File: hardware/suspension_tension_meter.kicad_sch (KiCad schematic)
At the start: 18 parts, among them J1 Conn_01x04, J2 Conn_01x06, J3 Conn_01x04, J4 Conn_01x04, SW1 Tactswitch, U1 STM32L4P5RET6, Y1 16MHz

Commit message: Arrange footprints
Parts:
- J1: footprint Connector_PinHeader_1.00mm:PinHeader_1x04_P1.00mm_Vertical_SMD_Pin1Left -> Connector_Wire:SolderWire-0.25sqmm_1x04_P4.2mm_D0.65mm_OD1.7mm_Relief
- J2: footprint Connector_PinHeader_1.00mm:PinHeader_1x06_P1.00mm_Vertical_SMD_Pin1Left -> Connector_PinHeader_2.54mm:PinHeader_1x06_P2.54mm_Vertical_SMD_Pin1Left
- J3, J4: footprint Connector_PinHeader_1.00mm:PinHeader_1x04_P1.00mm_Vertical_SMD_Pin1Left -> Connector_JST:JST_EH_S5B-EH_1x05_P2.50mm_Horizontal; symbol Connector_Generic:Conn_01x04 -> Connector_Generic:Conn_01x05
- SW1: footprint Button_Switch_SMD:SW_Push_1P1T_NO_6x6mm_H9.5mm -> Button_Switch_SMD:SW_SPST_PTS645
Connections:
- net GND: now also J3.5 (Pin_5), J4.5 (Pin_5)
- net SWO: now reaches J2.6 (Pin_6)
- net SWO: now also U1.55 (PB3)
- no-connect marks 40 -> 38
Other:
- note added: "SHLD"
- moved on the sheet: C1, C2, C3, C4, C5, J1, J2

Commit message: Apply PUTM branding
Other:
- company: PUT Motorsport -> Author: I. Kajdan
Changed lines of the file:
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@@
   (title_block
     (title "Push-rods Suspension Tension Meter")
-    (date "2022-12-10")
+    (date "2022-12-11")
     (rev "${REVISION}")
-    (company "PUT Motorsport")
-    (comment 3 "Reviewer:")
-    (comment 4 "Author: I. Kajdan")
+    (company "Author: I. Kajdan")
   )
   (junction (at 87.63 50.8) (diameter 0) (color 0 0 0 0)

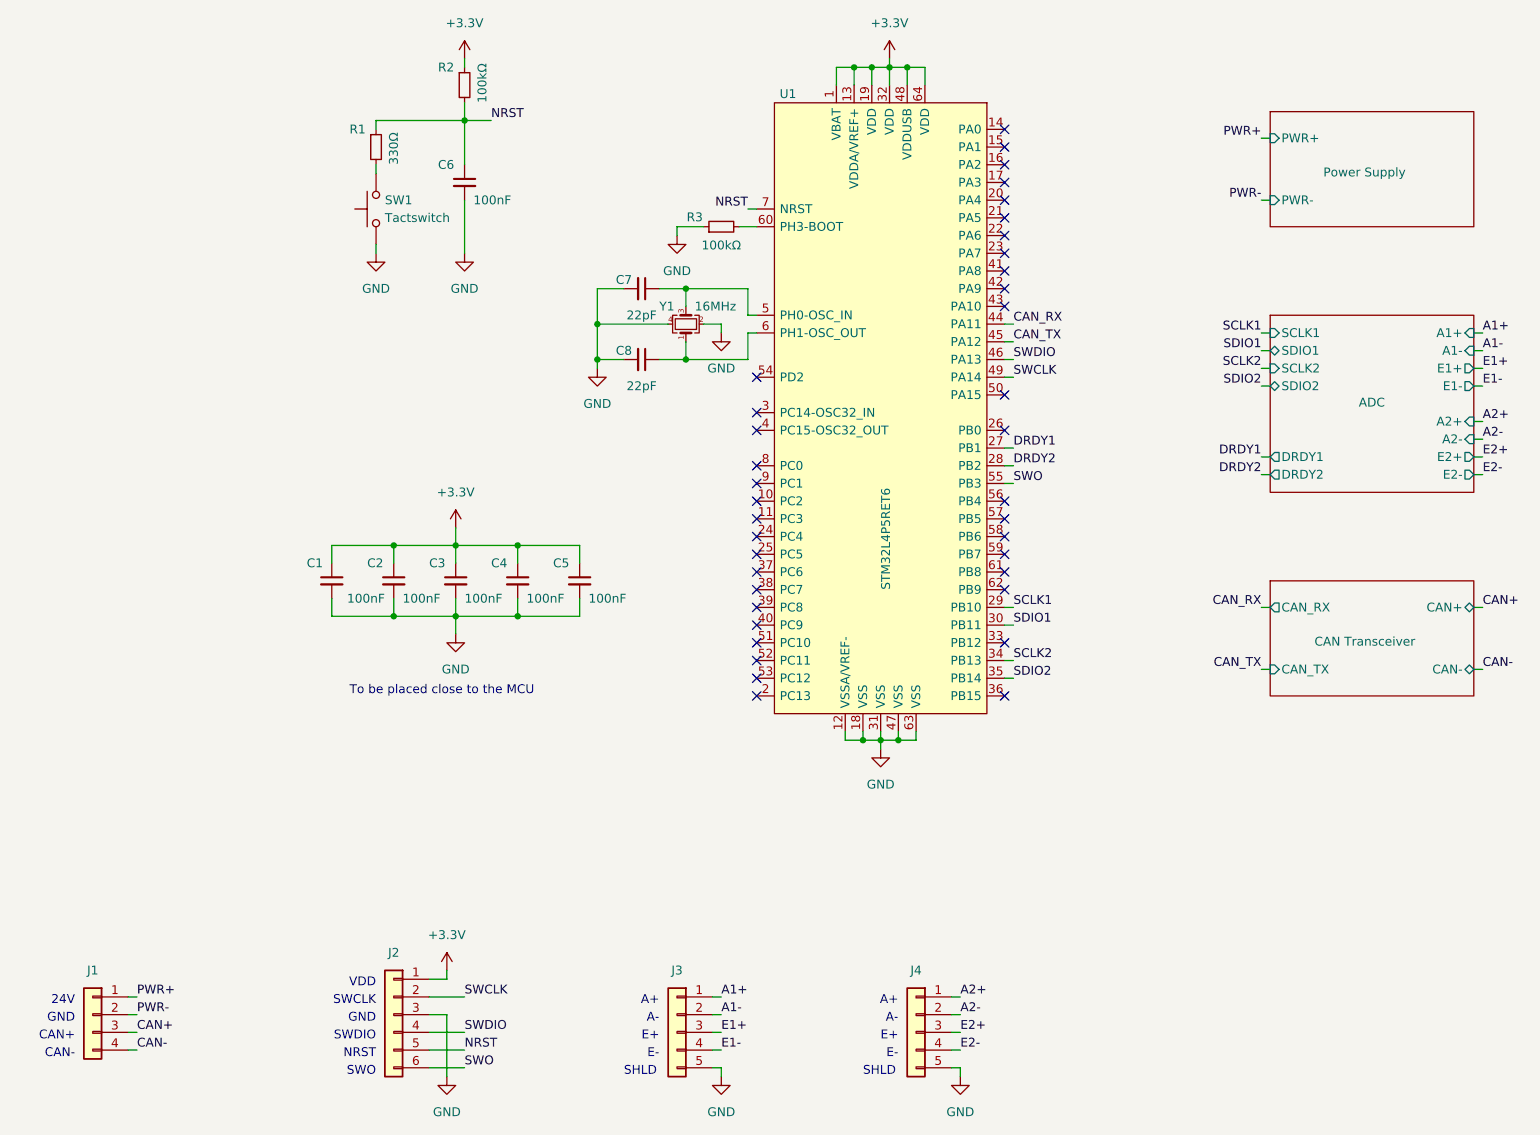
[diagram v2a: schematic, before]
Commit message: Miscellaneous changes
- Use THT connectors
- Adjust ADC circuit according to the datasheet
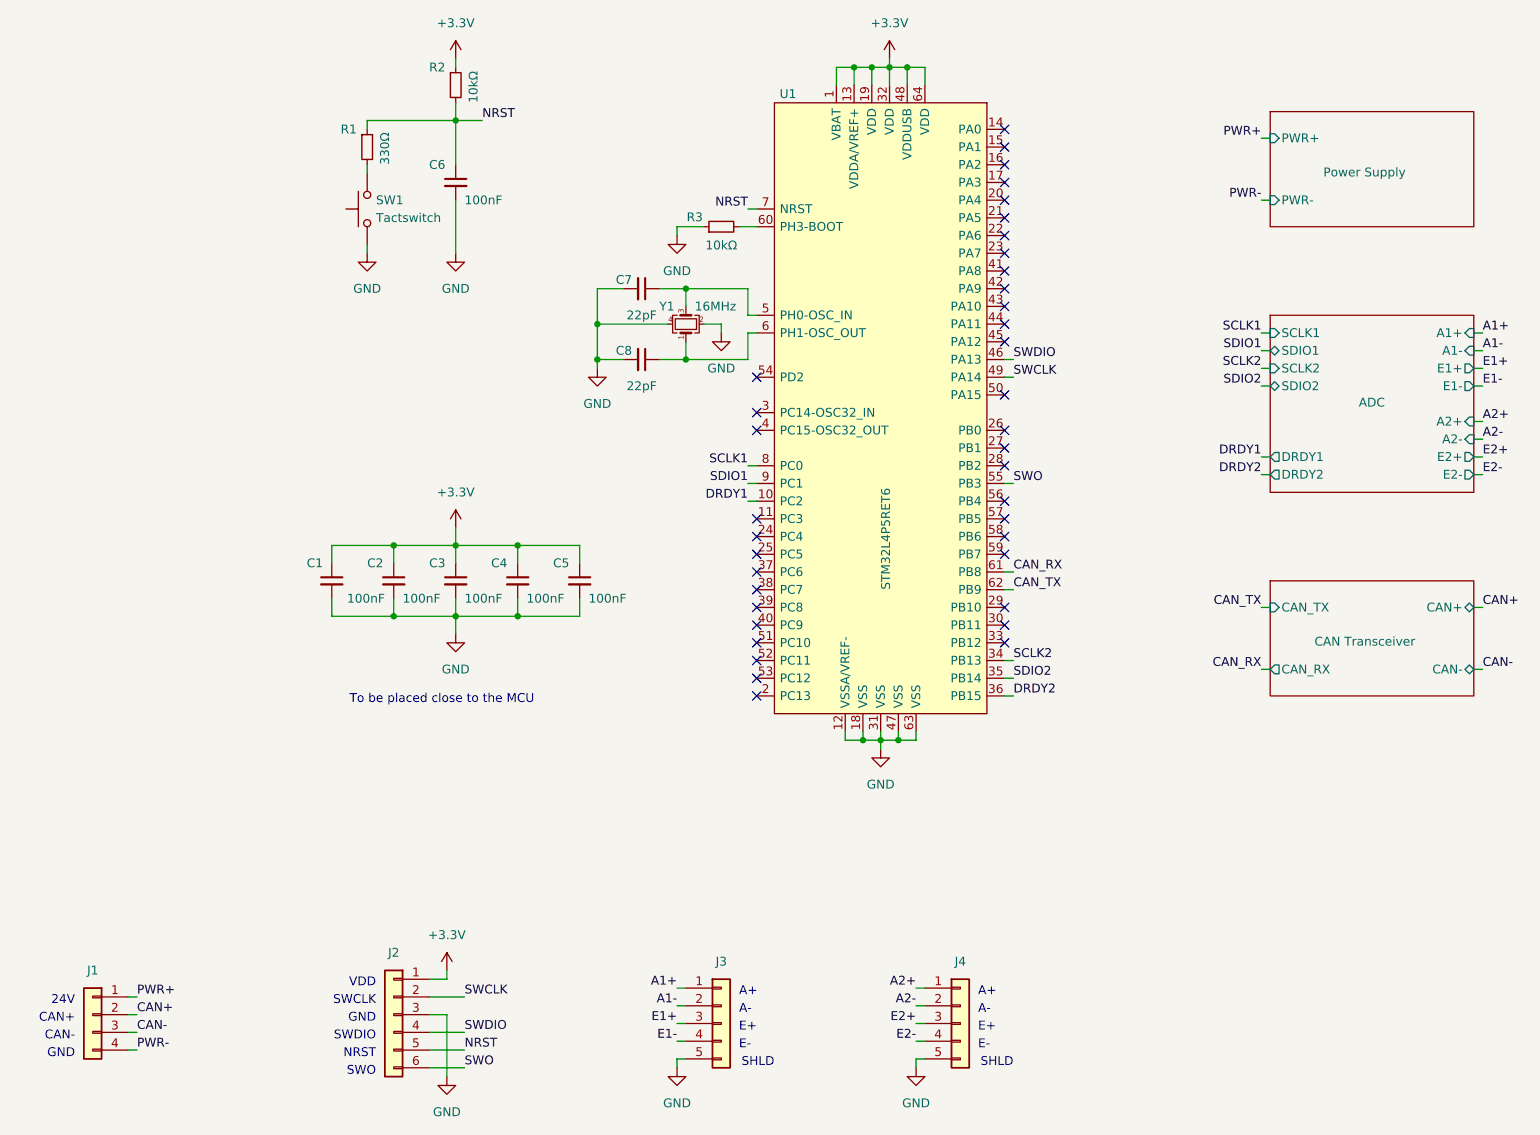
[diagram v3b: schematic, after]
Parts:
- J1: now left out of the parts list
- J2: footprint Connector_PinHeader_2.54mm:PinHeader_1x06_P2.54mm_Vertical_SMD_Pin1Left -> Connector_PinHeader_2.54mm:PinHeader_1x06_P2.54mm_Vertical
- J3, J4: footprint Connector_JST:JST_EH_S5B-EH_1x05_P2.50mm_Horizontal -> Connector_Molex:Molex_PicoBlade_53048-0510_1x05_P1.25mm_Horizontal
- R2, R3: value 100kΩ -> 10kΩ
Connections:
- net CAN+: now also J1.2 (Pin_2); no longer J1.3 (Pin_3)
- net CAN-: now also J1.3 (Pin_3); no longer J1.4 (Pin_4)
- net CAN_RX: now also U1.61 (PB8); no longer U1.44 (PA11)
- net CAN_TX: now also U1.62 (PB9); no longer U1.45 (PA12)
- net DRDY1: now also U1.10 (PC2); no longer U1.27 (PB1)
- net DRDY2: now also U1.36 (PB15); no longer U1.28 (PB2)
- net PWR-: now also J1.4 (Pin_4); no longer J1.2 (Pin_2)
- net SCLK1: now also U1.8 (PC0); no longer U1.29 (PB10)
- net SDIO1: now also U1.9 (PC1); no longer U1.30 (PB11)
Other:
- moved on the sheet: C6, J3, J4, R1, R2, SW1

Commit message: Route PCB tracks
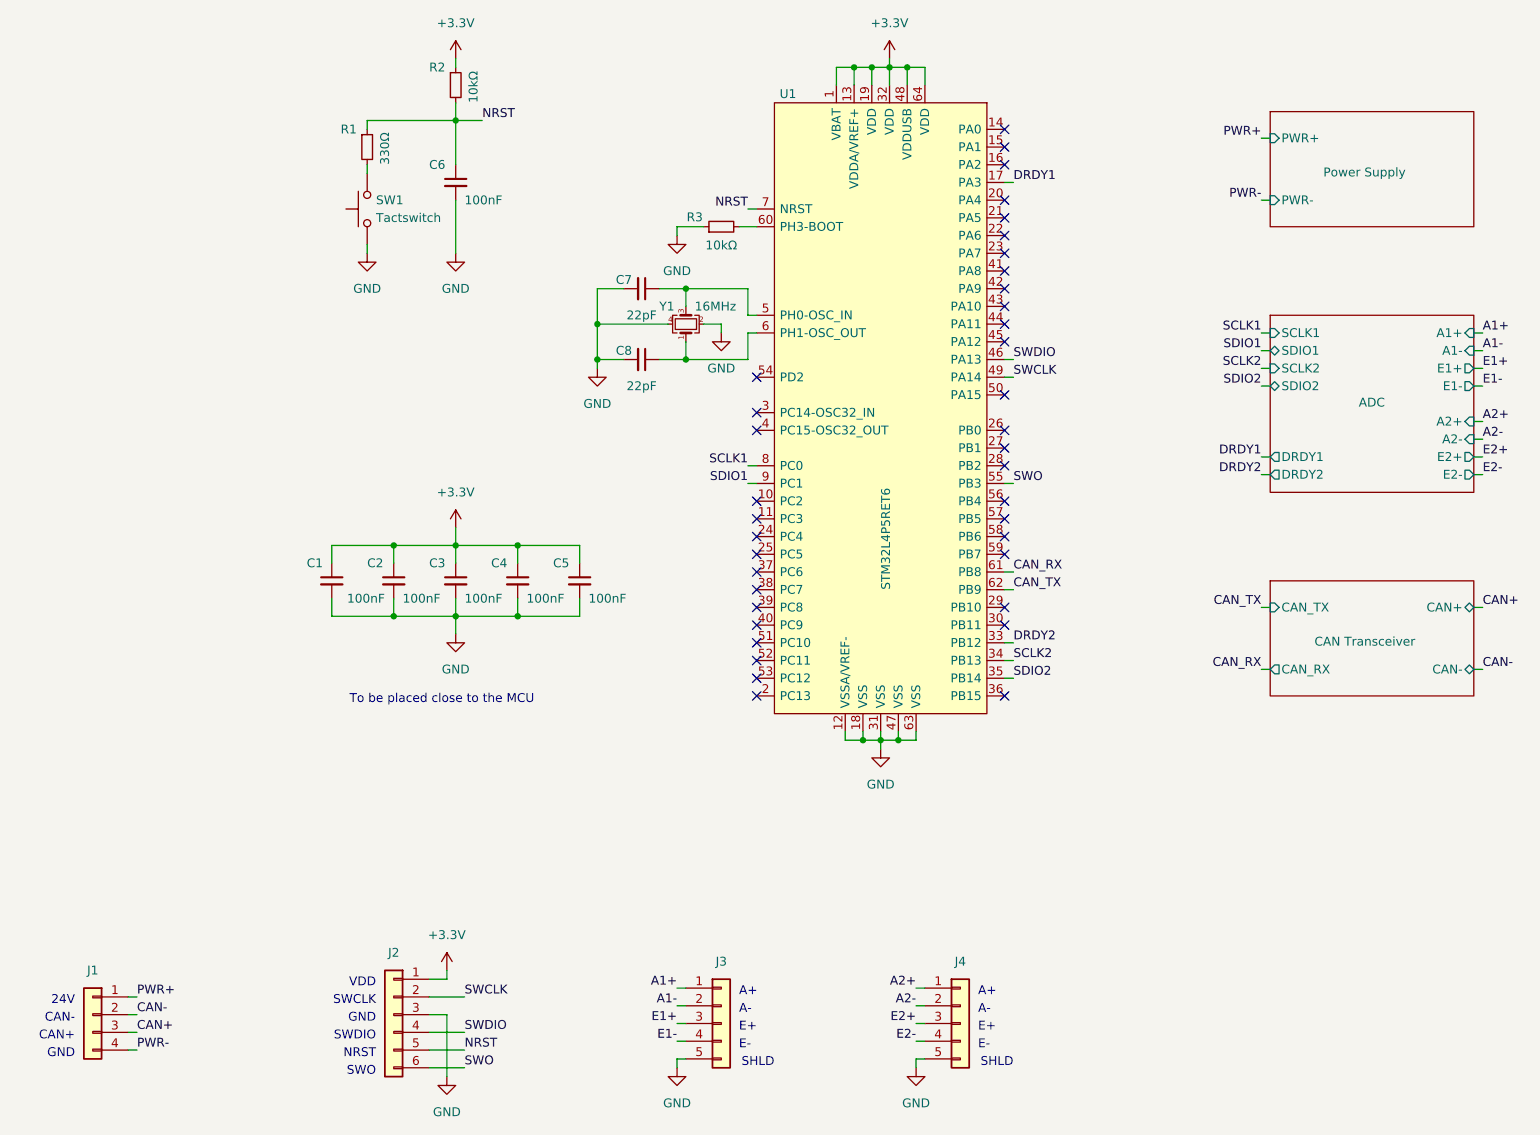
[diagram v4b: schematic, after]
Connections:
- net CAN+: now also J1.3 (Pin_3); no longer J1.2 (Pin_2)
- net CAN-: now also J1.2 (Pin_2); no longer J1.3 (Pin_3)
- net DRDY1: now also U1.17 (PA3); no longer U1.10 (PC2)
- net DRDY2: now also U1.33 (PB12); no longer U1.36 (PB15)
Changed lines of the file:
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@@
   (title_block
     (title "Push-rods Suspension Tension Meter")
-    (date "2022-12-11")
+    (date "2022-12-18")
     (rev "${REVISION}")
     (company "Author: I. Kajdan")
@@
   (no_connect (at 165.1 100.33))
   (no_connect (at 165.1 97.79))
-  (no_connect (at 165.1 125.73))
   (no_connect (at 165.1 123.19))
   (no_connect (at 165.1 120.65))
@@
   (no_connect (at 165.1 95.25))
   (no_connect (at 165.1 54.61))
-  (no_connect (at 165.1 57.15))
   (no_connect (at 165.1 52.07))
   (no_connect (at 165.1 62.23))
   (no_connect (at 165.1 64.77))
-  (no_connect (at 165.1 59.69))
   (no_connect (at 165.1 74.93))
   (no_connect (at 165.1 67.31))
@@
   (no_connect (at 165.1 72.39))
   (no_connect (at 165.1 77.47))
+  (no_connect (at 165.1 57.15))
+  (no_connect (at 165.1 133.35))
   (no_connect (at 165.1 82.55))
+  (no_connect (at 129.54 105.41))
   (wire (pts (xy 149.86 139.7) (xy 149.86 138.43))
     (stroke (width 0) (type default) (color 0 0 0 0))
@@
     (stroke (width 0) (type default) (color 0 0 0 0))
   )
+  (wire (pts (xy 165.1 59.69) (xy 166.37 59.69))
+    (stroke (width 0) (type default) (color 0 0 0 0))
+  )
   (wire (pts (xy 121.92 80.01) (xy 124.46 80.01))
     (stroke (width 0) (type default) (color 0 0 0 0))
@@
     (stroke (width 0) (type default) (color 0 0 0 0))
   )
-  (wire (pts (xy 166.37 133.35) (xy 165.1 133.35))
+  (wire (pts (xy 166.37 125.73) (xy 165.1 125.73))
     (stroke (width 0) (type default) (color 0 0 0 0))
   )
@@
     (stroke (width 0) (type default) (color 0 0 0 0))
   )
-  (wire (pts (xy 129.54 105.41) (xy 128.27 105.41))
-    (stroke (width 0) (type default) (color 0 0 0 0))
-  )
   (wire (pts (xy 86.36 121.92) (xy 77.47 121.92))
     (stroke (width 0) (type default) (color 0 0 0 0))
@@
     (effects (font (size 1.27 1.27)) (justify left bottom))
   )
-  (text "CAN+" (at 31.75 180.34 180)
+  (text "CAN+" (at 31.75 182.88 180)
     (effects (font (size 1.27 1.27)) (justify right bottom))
   )
@@
     (effects (font (size 1.27 1.27)) (justify left bottom))
   )
-  (text "CAN-" (at 31.75 182.88 180)
+  (text "CAN-" (at 31.75 180.34 180)
     (effects (font (size 1.27 1.27)) (justify right bottom))
   )
@@
     (effects (font (size 1.27 1.27)) (justify left bottom))
   )
-  (label "CAN+" (at 40.64 179.07 0)
+  (label "CAN-" (at 40.64 179.07 0)
     (effects (font (size 1.27 1.27)) (justify left bottom))
   )
@@
     (effects (font (size 1.27 1.27)) (justify right bottom))
   )
-  (label "DRDY1" (at 128.27 105.41 180)
-    (effects (font (size 1.27 1.27)) (justify right bottom))
-  )
   (label "NRST" (at 87.63 184.15 0)
     (effects (font (size 1.27 1.27)) (justify left bottom))
@@
     (effects (font (size 1.27 1.27)) (justify right bottom))
   )
-  (label "CAN-" (at 40.64 181.61 0)
+  (label "CAN+" (at 40.64 181.61 0)
     (effects (font (size 1.27 1.27)) (justify left bottom))
   )
@@
     (effects (font (size 1.27 1.27)) (justify right bottom))
   )
-  (label "DRDY2" (at 166.37 133.35 0)
+  (label "DRDY2" (at 166.37 125.73 0)
     (effects (font (size 1.27 1.27)) (justify left bottom))
   )
@@
     (effects (font (size 1.27 1.27)) (justify right bottom))
   )
+  (label "DRDY1" (at 166.37 59.69 0)
+    (effects (font (size 1.27 1.27)) (justify left bottom))
+  )
   (label "CAN_TX" (at 166.37 118.11 0)

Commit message: Release v1.0.0
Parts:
- renumbered C6 to C1, C7 to C2, C8 to C3, C1 to C4, C2 to C5, C3 to C6, C4 to C7, C5 to C8, R2 to R1, R1 to R2
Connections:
- net PWR- is gone; now on net GND: J1.4 (Pin_4)
- net PWR+ renamed +24V
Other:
- sheet Power Supply ports: added +24V, GND; removed PWR+, PWR-
